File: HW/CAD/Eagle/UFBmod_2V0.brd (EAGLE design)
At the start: 98.4 x 89.5 mm, 165 parts, among them T0551 MMBT2222, U0501 MIDAS_MCCOG21605B6W-FPTLWI, U0601 MAX5217, U0701 AT86RF215-ZU, U0711 ASVTX-13-D-26.000MHZ-I05-T, U0811 PE4259, U0821 RFX1010, U0881 B39871B3440U410, U0911 FT232HL, U1101 TPS53353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

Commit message: HW_2V0 - HW/CAD/Eagle - all parts placed for the first time
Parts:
- moved D0971 341.0 mm to (45.7, 83.8), turned to 90 degrees
- moved D0972 327.6 mm to (40.6, 83.8), turned to 90 degrees
- moved R0968 300.0 mm to (69.8, 66.0), turned to 270 degrees
- moved R0967 294.6 mm to (67.9, 66.0), turned to 270 degrees
- moved R0966 289.2 mm to (66.0, 66.0), turned to 270 degrees
- moved R0972 279.9 mm to (67.3, 35.6), flipped to the bottom, turned to 270 degrees
- moved R0964 279.1 mm to (64.8, 66.0), turned to 270 degrees
- moved R0971 275.5 mm to (68.6, 35.6), flipped to the bottom, turned to 270 degrees
- moved R0962 269.1 mm to (63.5, 66.0), turned to 270 degrees
- moved R0965 265.9 mm to (73.7, 43.8), flipped to the bottom, turned to 180 degrees
- moved R0941 261.2 mm to (68.6, 66.0), flipped to the bottom, turned to 90 degrees
- moved R0963 257.6 mm to (73.7, 45.1), flipped to the bottom, turned to 180 degrees
- moved R0961 249.4 mm to (73.7, 46.4), flipped to the bottom
- moved C0921 232.4 mm to (70.5, 44.5), turned to 180 degrees
- moved R0931 232.0 mm to (58.4, 43.8), flipped to the bottom
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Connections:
- net FPGA_FT_12MHZ: now also JB2.99
- net FPGA_FT_CTS: now also JB2.87
- net FPGA_FT_DCD: now also JB2.95
- net FPGA_FT_DSR: now also JB2.93
- net FPGA_FT_DTR: now also JB2.91
- net FPGA_FT_RESET: now also JB2.77
- net FPGA_FT_RI: now also JB2.97
- net FPGA_FT_RTS: now also JB2.85
- net FPGA_FT_RXD: now also JB2.83
- net FPGA_FT_TXD: now also JB2.81
- net FPGA_RFX_MODE: now also JB2.75
- net RFX_TXEN: now also U0811.4
- net TRX_FEA09: no longer U0811.4
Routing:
- net TRX_FEB09: track 18.7 -> 0.00 mm, vias 2 -> 0
- net TRX_FEA09: track 17.0 -> 6.71 mm
- net +3V3: track 27.9 -> 27.3 mm

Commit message: HW_2V0 - HW/CAD/Eagle - work of the day
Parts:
- added C1350: 100nF, df4iah_rcl:C0402
- added R1351, R1352, R1353, R1354, R1355, R1356, R1357, R1358, R1361, R1362, R1363, R1364, R1365, R1366, R1367, R1368, R1371, R1372, R1373, R1374, R1375, R1376: 100R, df4iah_rcl:R0402
- added X1350: (no value), df4iah_connector:2X03
- moved R1023 1.27 mm to (27.3, 20.3), flipped to the top
- moved R1022 0.64 mm to (26.0, 20.3), flipped to the top
- flipped R1021 to the top
- renumbered X1321 to X1351, X1322 to X1361, X1323 to X1371
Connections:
- new net B2W_51: R1351.2, X1351.1
- new net B2W_52: R1352.2, X1351.2
- new net B2W_53: R1353.2, X1351.3
- new net B2W_54: R1354.2, X1351.4
- new net B2W_55: R1355.2, X1351.5
- new net B2W_56: R1356.2, X1351.6
- new net B2W_57: R1357.2, X1351.7
- new net B2W_58: R1358.2, X1351.8
- new net B2W_61: R1361.2, X1361.1
- new net B2W_62: R1362.2, X1361.2
- new net B2W_63: R1363.2, X1361.3
- new net B2W_64: R1364.2, X1361.4
- new net B2W_65: R1365.2, X1361.5
- new net B2W_66: R1366.2, X1361.6
- new net B2W_67: R1367.2, X1361.7
- new net B2W_68: R1368.2, X1361.8
- new net B2W_71: R1371.2, X1371.1
- new net B2W_72: R1372.2, X1371.2
- new net B2W_73: R1373.2, X1371.3
- new net B2W_74: R1374.2, X1371.4
- new net B2W_75: R1375.2, X1371.5
- new net B2W_76: R1376.2, X1371.6
- new net FPGA_B16_L10_N: JB1.69, R1368.1
- new net FPGA_B16_L10_P: JB1.71, R1367.1
- new net FPGA_B16_L11_N: JB1.67, R1366.1
- new net FPGA_B16_L11_P: JB1.65, R1365.1
- new net FPGA_B16_L16_N: JB1.37, R1352.1
- new net FPGA_B16_L16_P: JB1.35, R1351.1
- new net FPGA_B16_L17_N: JB1.45, R1356.1
- new net FPGA_B16_L17_P: JB1.47, R1355.1
- new net FPGA_B16_L18_N: JB1.49, R1358.1
- new net FPGA_B16_L18_P: JB1.51, R1357.1
- new net FPGA_B16_L19_N: JB1.39, R1354.1
- new net FPGA_B16_L19_P: JB1.41, R1353.1
- new net FPGA_B16_L2_N: JB1.79, R1374.1
- new net FPGA_B16_L2_P: JB1.81, R1373.1
- new net FPGA_B16_L5_N: JB1.75, R1372.1
- new net FPGA_B16_L5_P: JB1.77, R1371.1
- new net FPGA_B16_L6_N: JB1.85, R1376.1
- new net FPGA_B16_L6_P: JB1.87, R1375.1
- new net FPGA_B16_L7_N: JB1.59, R1364.1
- new net FPGA_B16_L7_P: JB1.61, R1363.1
- new net FPGA_B16_L9_N: JB1.55, R1362.1
- new net FPGA_B16_L9_P: JB1.57, R1361.1
- new net VCCIO16: C1350.2, JB1.10, JB1.12, X1350.1, X1350.3, X1350.5
- net +2V5: now also X1350.4
- net GND: now also C1350.1
- net U1V8: now also X1350.2
- net U3V3: now also X1350.6; no longer JB1.10, JB1.12
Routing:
- net TPS_VIN: track 0.00 -> 17.6 mm
- net GND: track 67.1 -> 82.6 mm, vias 33 -> 34
- net B2W_68: track 0.00 -> 7.13 mm
- net B2W_58: track 0.00 -> 7.13 mm
- net B2W_72: track 0.00 -> 7.05 mm
- net B2W_56: track 0.00 -> 7.05 mm
- net B2W_76: track 0.00 -> 7.05 mm
- net B2W_66: track 0.00 -> 7.05 mm
- net B2W_62: track 0.00 -> 7.05 mm
- net B2W_52: track 0.00 -> 7.05 mm
- net B2W_74: track 0.00 -> 6.97 mm
- net B2W_64: track 0.00 -> 6.97 mm
- net B2W_54: track 0.00 -> 6.97 mm
- net VIN_PWR: track 0.00 -> 6.12 mm
- net LED_RGB_BLUE: track 0.00 -> 6.00 mm
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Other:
- board text added: "1.8V"
- board text added: "2.5V"
- board text added: "3.3V"
- board text added: "VCCIO16"

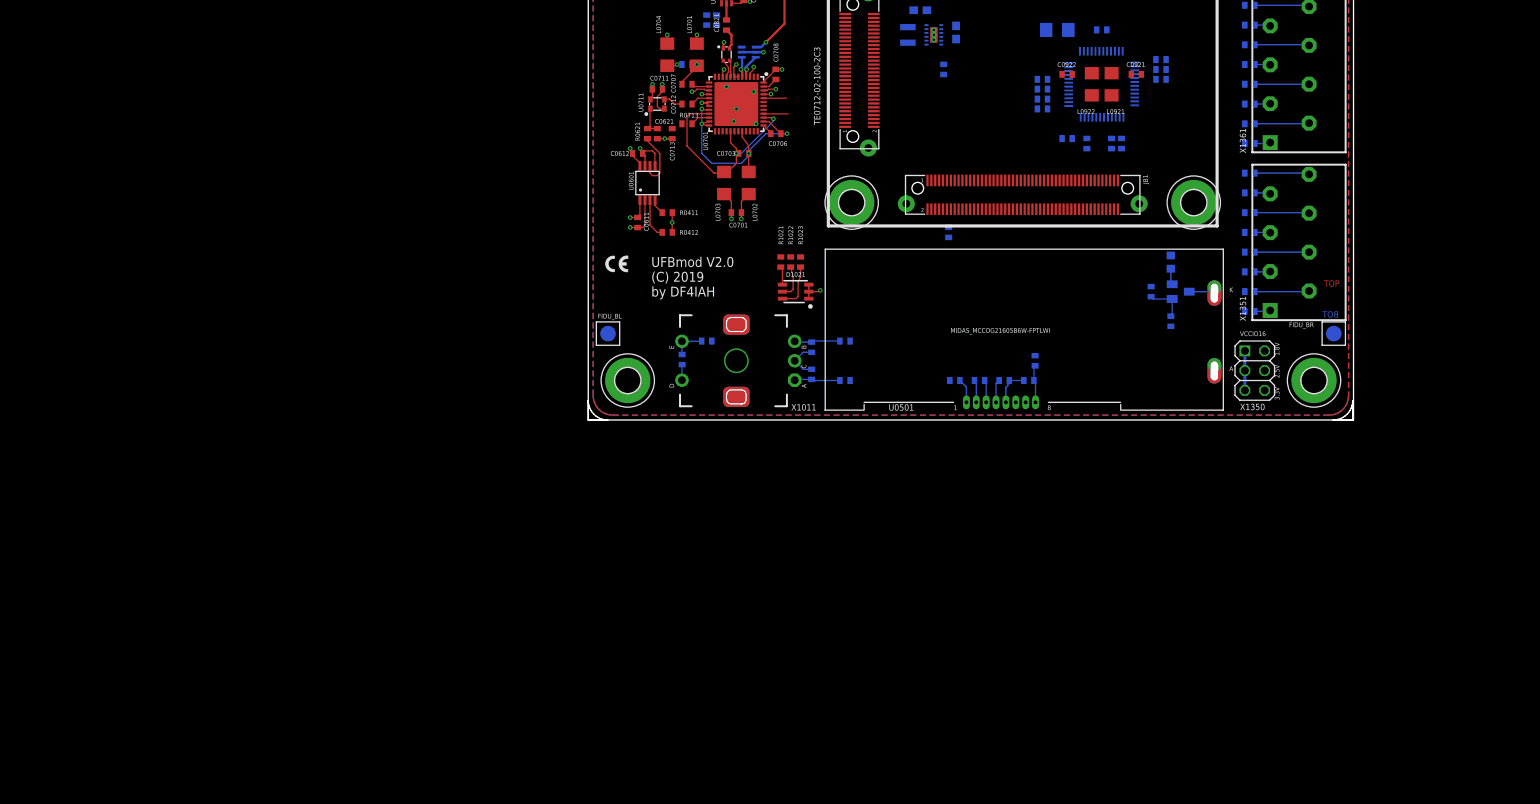
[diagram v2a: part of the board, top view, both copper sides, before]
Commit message: HW_2V0 - HW/CAD/Eagle - ARJE-0034 added
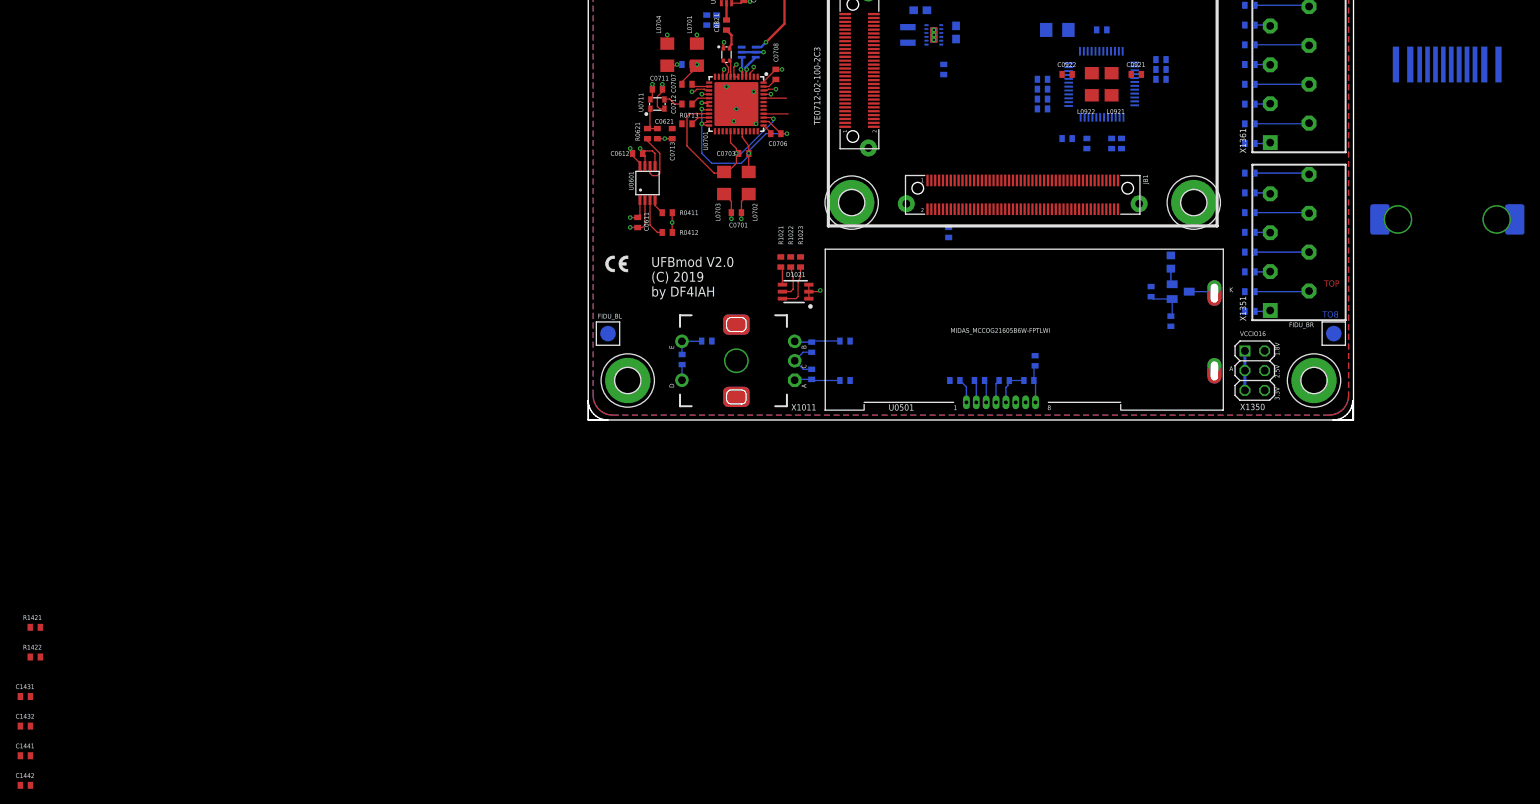
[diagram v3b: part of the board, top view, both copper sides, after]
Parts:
- added C1431, C1441: 1uF, df4iah_rcl:C0402
- added C1432, C1442: 100nF, df4iah_rcl:C0402
- added J1411: (no value), df4iah_connector:ARJE-0034_RJ45_WITH_MAGNETICS
- added R1421, R1422: 1kR, df4iah_rcl:R0402
- renumbered H1411 to H1511, H1412 to H1512, H1413 to H1513, H1414 to H1514
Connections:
- new net ETH_DA_G: J1411.12, R1422.2
- new net ETH_DA_Y: J1411.1, R1421.2
- new net FPGA_ETH_DA_G: R1422.1
- new net FPGA_ETH_DA_Y: R1421.1
- net +3V3: now also C1431.1, C1432.1, C1441.1, C1442.1, J1411.5, J1411.6
- net FPGA_ETH_RD_N: now also J1411.8
- net FPGA_ETH_RD_P: now also J1411.7
- net FPGA_ETH_TD_N: now also J1411.4
- net FPGA_ETH_TD_P: now also J1411.3
- net GND: now also C1431.2, C1432.2, C1441.2, C1442.2, J1411.10, J1411.11, J1411.2, J1411.GND@11, J1411.GND@12, J1411.GND@21, J1411.GND@22
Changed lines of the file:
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@@
 <setting verticaltext="up"/>
 </settings>
-<grid distance="50" unitdist="mil" unit="mm" style="dots" multiple="1" display="yes" altdistance="12.5" altunitdist="mil" altunit="mil"/>
+<grid distance="50" unitdist="mil" unit="mil" style="dots" multiple="1" display="yes" altdistance="12.5" altunitdist="mil" altunit="mil"/>
 <layers>
 <layer number="1" name="Top" color="4" fill="1" visible="yes" active="yes"/>
@@
 </autorouter>
 <elements>
-<element name="H1411" library="df4iah_holes" package="3,2-PAD" value="MOUNT-PAD-ROUND3.2" x="5.08" y="84.455" locked="yes" smashed="yes"/>
-<element name="H1413" library="df4iah_holes" package="3,2-PAD" value="MOUNT-PAD-ROUND3.2" x="93.345" y="84.455" locked="yes" smashed="yes"/>
-<element name="H1412" library="df4iah_holes" package="3,2-PAD" value="MOUNT-PAD-ROUND3.2" x="5.08" y="5.08" locked="yes" smashed="yes"/>
-<element name="H1414" library="df4iah_holes" package="3,2-PAD" value="MOUNT-PAD-ROUND3.2" x="93.345" y="5.08" locked="yes" smashed="yes"/>
+<element name="H1511" library="df4iah_holes" package="3,2-PAD" value="MOUNT-PAD-ROUND3.2" x="5.08" y="84.455" locked="yes" smashed="yes"/>
+<element name="H1513" library="df4iah_holes" package="3,2-PAD" value="MOUNT-PAD-ROUND3.2" x="93.345" y="84.455" locked="yes" smashed="yes"/>
+<element name="H1512" library="df4iah_holes" package="3,2-PAD" value="MOUNT-PAD-ROUND3.2" x="5.08" y="5.08" locked="yes" smashed="yes"/>
+<element name="H1514" library="df4iah_holes" package="3,2-PAD" value="MOUNT-PAD-ROUND3.2" x="93.345" y="5.08" locked="yes" smashed="yes"/>
 <element name="L1101" library="df4iah_rcl" package="L1812" value="440nH" x="73.18375" y="72.86625" smashed="yes" rot="R90">
 <attribute name="NAME" x="75.72375" y="73.739375" size="0.6096" layer="25" font="vector" ratio="10" rot="R270"/>
@@
 <attribute name="VALUE" x="44.7675" y="22.86" size="0.6096" layer="28" font="vector" ratio="10" rot="MR90"/>
 </element>
+<element name="J1411" library="df4iah_connector" package="ARJE-0034_RJ45_WITH_MAGNETICS" value="" x="110.49" y="34.29" rot="MR0"/>
+<element name="R1421" library="df4iah_rcl" package="R0402" value="1kR" x="-71.12" y="-26.67"/>
+<element name="R1422" library="df4iah_rcl" package="R0402" value="1kR" x="-71.12" y="-30.48"/>
+<element name="C1431" library="df4iah_rcl" package="C0402" value="1uF" x="-72.39" y="-35.56"/>
+<element name="C1432" library="df4iah_rcl" package="C0402" value="100nF" x="-72.39" y="-39.37"/>
+<element name="C1441" library="df4iah_rcl" package="C0402" value="1uF" x="-72.39" y="-43.18"/>
+<element name="C1442" library="df4iah_rcl" package="C0402" value="100nF" x="-72.39" y="-46.99"/>
 </elements>
 <signals>
 <signal name="GND">
-<contactref element="H1411" pad="B3,2"/>
-<contactref element="H1412" pad="B3,2"/>
-<contactref element="H1413" pad="B3,2"/>
-<contactref element="H1414" pad="B3,2"/>
+<contactref element="H1511" pad="B3,2"/>
+<contactref element="H1512" pad="B3,2"/>
+<contactref element="H1513" pad="B3,2"/>
+<contactref element="H1514" pad="B3,2"/>
 <contactref element="C1153" pad="2"/>
 <contactref element="L0701" pad="1"/>
@@
 <wire x1="27.64625" y1="6.52375" x2="26.55" y2="7.62" width="0.1524" layer="16"/>
 <via x="29.845" y="16.66875" extent="1-16" drill="0.3"/>
+<wire x1="28.37" y1="16.51" x2="29.68625" y2="16.51" width="0.1524" layer="1"/>
+<wire x1="29.68625" y1="16.51" x2="29.845" y2="16.66875" width="0.1524" layer="1"/>
+<contactref element="J1411" pad="GND@11"/>
+<contactref element="J1411" pad="GND@21"/>
+<contactref element="J1411" pad="GND@12"/>
+<contactref element="J1411" pad="GND@22"/>
+<contactref element="J1411" pad="10"/>
+<contactref element="J1411" pad="11"/>
+<contactref element="J1411" pad="2"/>
+<contactref element="C1431" pad="2"/>
+<contactref element="C1432" pad="2"/>
+<contactref element="C1441" pad="2"/>
+<contactref element="C1442" pad="2"/>
 <wire x1="92.71" y1="74.77" x2="93.345" y2="84.455" width="0" layer="19" extent="1-1"/>
 <wire x1="83.5" y1="76.2" x2="92.71" y2="74.77" width="0" layer="19" extent="1-1"/>
@@
 <wire x1="53.715" y1="4.185" x2="46.49875" y2="5.08" width="0" layer="19" extent="16-16"/>
 <wire x1="93.345" y1="5.08" x2="74.93" y2="12.05" width="0" layer="19" extent="16-16"/>
-<wire x1="28.37" y1="16.51" x2="29.68625" y2="16.51" width="0.1524" layer="1"/>
-<wire x1="29.68625" y1="16.51" x2="29.845" y2="16.66875" width="0.1524" layer="1"/>
+<wire x1="101.8159" y1="25.7937" x2="5.08" y2="5.08" width="0" layer="19" extent="1-1"/>
+<wire x1="104.14" y1="25.7937" x2="101.8159" y2="25.7937" width="0" layer="19" extent="1-1"/>
+<wire x1="116.84" y1="25.7937" x2="104.14" y2="25.7937" width="0" layer="19" extent="1-1"/>
+<wire x1="119.1641" y1="25.7937" x2="116.84" y2="25.7937" width="0" layer="19" extent="1-1"/>
+<wire x1="115.2398" y1="45.72" x2="116.84" y2="25.7937" width="0" layer="19" extent="1-1"/>
+<wire x1="114.046" y1="45.72" x2="115.2398" y2="45.72" width="0" layer="19" extent="1-1"/>
+<wire x1="105.7148" y1="45.72" x2="114.046" y2="45.72" width="0" layer="19" extent="1-1"/>
+<wire x1="-71.74" y1="-35.56" x2="119.1641" y2="25.7937" width="0" layer="19" extent="1-1"/>
+<wire x1="-71.74" y1="-39.37" x2="-71.74" y2="-35.56" width="0" layer="19" extent="1-1"/>
+<wire x1="-71.74" y1="-43.18" x2="-71.74" y2="-39.37" width="0" layer="19" extent="1-1"/>
+<wire x1="-71.74" y1="-46.99" x2="-71.74" y2="-43.18" width="0" layer="19" extent="1-1"/>
 </signal>
 <signal name="+3V3">
@@
 <wire x1="52.84875" y1="5.08" x2="52.445" y2="4.67625" width="0.1524" layer="16"/>
 <wire x1="52.445" y1="4.67625" x2="52.445" y2="2.27" width="0.1524" layer="16"/>
+<contactref element="J1411" pad="5"/>
+<contactref element="J1411" pad="6"/>
+<contactref element="C1431" pad="1"/>
+<contactref element="C1432" pad="1"/>
+<contactref element="C1441" pad="1"/>
+<contactref element="C1442" pad="1"/>
 <wire x1="77.47" y1="71.44" x2="80.01" y2="71.44" width="0" layer="19" extent="1-1"/>
 <wire x1="73.18375" y1="70.91625" x2="77.47" y2="71.44" width="0" layer="19" extent="1-1"/>
@@
 <wire x1="52.84875" y1="5.08" x2="47.13" y2="27.11" width="0" layer="19" extent="1-16"/>
 <wire x1="80.53" y1="5.57" x2="52.84875" y2="5.08" width="0" layer="19" extent="1-16"/>
+<wire x1="108.966" y1="45.72" x2="5.3975" y2="26.035" width="0" layer="19" extent="1-1"/>
+<wire x1="109.982" y1="45.72" x2="108.966" y2="45.72" width="0" layer="19" extent="1-1"/>
+<wire x1="-73.04" y1="-35.56" x2="109.982" y2="45.72" width="0" layer="19" extent="1-1"/>
+<wire x1="-73.04" y1="-39.37" x2="-73.04" y2="-35.56" width="0" layer="19" extent="1-1"/>
+<wire x1="-73.04" y1="-43.18" x2="-73.04" y2="-39.37" width="0" layer="19" extent="1-1"/>
+<wire x1="-73.04" y1="-46.99" x2="-73.04" y2="-43.18" width="0" layer="19" extent="1-1"/>
 </signal>
 <signal name="P$8">
@@
 <signal name="FPGA_ETH_TD_P">
 <contactref element="JB1" pad="3"/>
+<contactref element="J1411" pad="3"/>
+<wire x1="106.934" y1="45.72" x2="44.13" y2="30.81" width="0" layer="19" extent="1-1"/>
 </signal>
 <signal name="FPGA_ETH_TD_N">
 <contactref element="JB1" pad="5"/>
+<contactref element="J1411" pad="4"/>
+<wire x1="107.95" y1="45.72" x2="44.63" y2="30.81" width="0" layer="19" extent="1-1"/>
 </signal>
 <signal name="FPGA_ETH_RD_P">
 <contactref element="JB1" pad="9"/>
+<contactref element="J1411" pad="7"/>
+<wire x1="110.998" y1="45.72" x2="45.63" y2="30.81" width="0" layer="19" extent="1-1"/>
 </signal>
 <signal name="FPGA_ETH_RD_N">
 <contactref element="JB1" pad="11"/>
+<contactref element="J1411" pad="8"/>
+<wire x1="112.014" y1="45.72" x2="46.13" y2="30.81" width="0" layer="19" extent="1-1"/>
 </signal>
 <signal name="U1V5">
@@
 <wire x1="45.63" y1="27.11" x2="46.13" y2="27.11" width="0" layer="19" extent="1-1"/>
 </signal>
+<signal name="ETH_DA_Y">
+<contactref element="J1411" pad="1"/>
+<contactref element="R1421" pad="2"/>
+<wire x1="103.886" y1="45.72" x2="-70.47" y2="-26.67" width="0" layer="19" extent="1-1"/>
+</signal>
+<signal name="ETH_DA_G">
+<contactref element="J1411" pad="12"/>
+<contactref element="R1422" pad="2"/>
+<wire x1="117.0686" y1="45.72" x2="-70.47" y2="-30.48" width="0" layer="19" extent="1-1"/>
+</signal>
+<signal name="FPGA_ETH_DA_G">
+<contactref element="R1422" pad="1"/>
+</signal>
+<signal name="FPGA_ETH_DA_Y">
+<contactref element="R1421" pad="1"/>
+</signal>
 </signals>
